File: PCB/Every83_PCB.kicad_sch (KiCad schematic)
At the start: 36 parts, among them IC2 GD25Q16, J1 781710004, J2 Conn_01x08_Pin, Q3 DMG2305, SW101 KMR2, SW102 KMR2, U2 AP2112(3.3V), U3 MCP73831T-2ACI/OT, X3 JSTPH, Y2 32.768

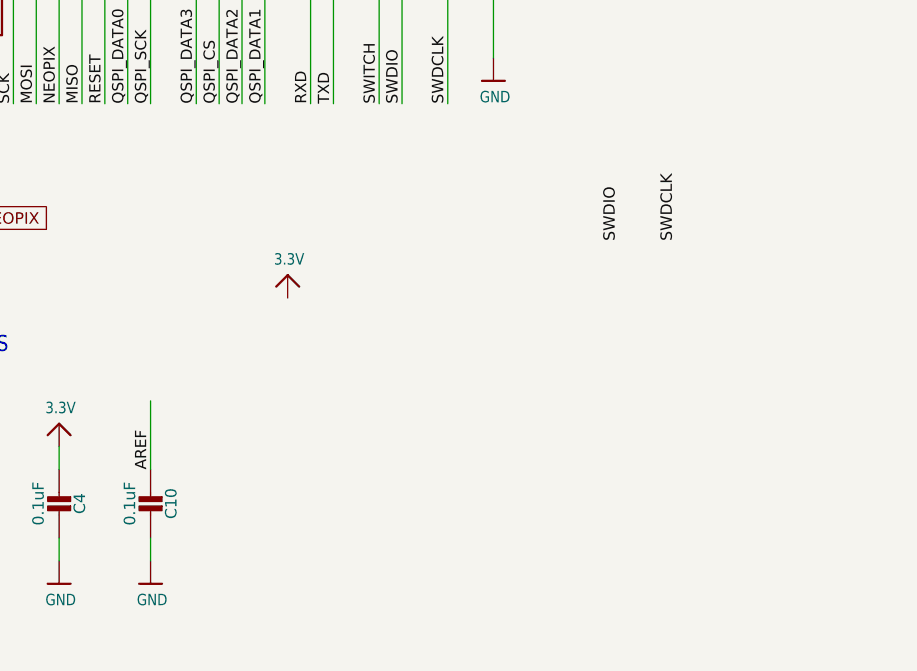
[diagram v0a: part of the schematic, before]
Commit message: update matrix nets and add swd footprint
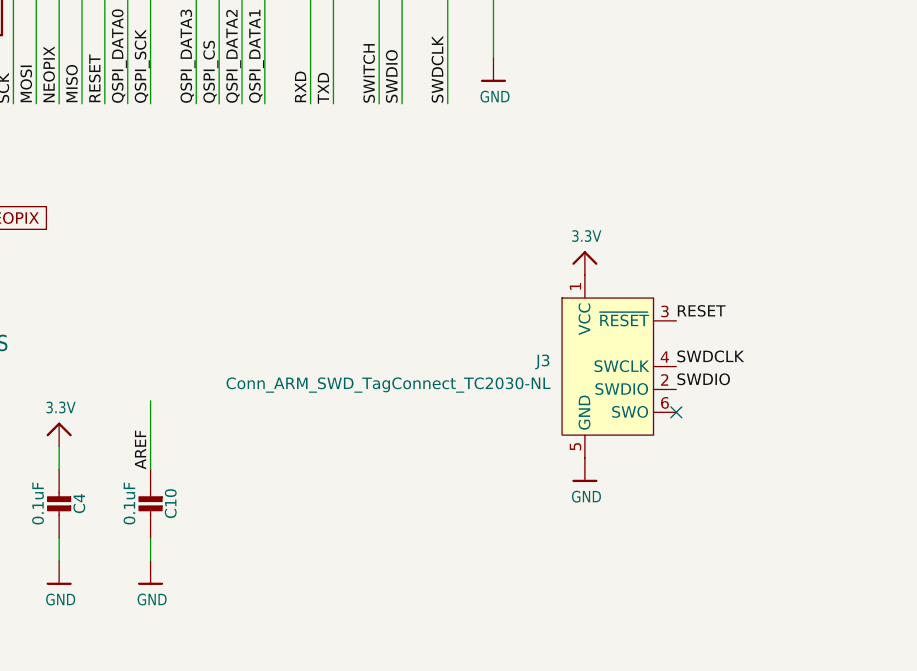
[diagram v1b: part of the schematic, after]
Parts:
- added J3: Conn_ARM_SWD_TagConnect_TC2030-NL, Connector:Tag-Connect_TC2030-IDC-NL_2x03_P1.27mm_Vertical, symbol Connector:Conn_ARM_SWD_TagConnect_TC2030-NL
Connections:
- net 3.3V: now also J3.1 (VCC)
- net GND: now also J3.5 (GND)
- net RESET: now also J3.3 (~{RESET})
- net SWDCLK: now also J3.4 (SWCLK)
- net SWDIO: now also J3.2 (SWDIO)
- no-connect marks 0 -> 1
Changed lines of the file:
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@@
   (junction (at 40.64 187.96) (diameter 0) (color 0 0 0 0)
   )
+  (no_connect (at 200.66 179.07))
   (wire (pts (xy 170.18 129.54) (xy 170.18 144.78))
     (stroke (width 0) (type default))
@@
     (effects (font (size 1.2446 1.2446)) (justify left bottom))
   )
+  (label "RESET" (at 200.66 168.91 0) (fields_autoplaced)
+    (effects (font (size 1.2446 1.2446)) (justify left bottom))
+  )
   (label "CS" (at 260.35 143.51 0) (fields_autoplaced)
     (effects (font (size 1.27 1.27)) (justify left bottom))
@@
     (effects (font (size 1.2446 1.2446)) (justify left bottom))
   )
-  (label "SWDIO" (at 194.31 160.02 90) (fields_autoplaced)
+  (label "SWDIO" (at 200.66 176.53 0) (fields_autoplaced)
     (effects (font (size 1.27 1.27)) (justify left bottom))
   )
@@
     (effects (font (size 1.27 1.27)) (justify left bottom))
   )
-  (label "SWDCLK" (at 200.66 160.02 90) (fields_autoplaced)
+  (label "SWDCLK" (at 200.66 173.99 0) (fields_autoplaced)
     (effects (font (size 1.27 1.27)) (justify left bottom))
   )
@@
         (path "/ea2432c4-eb7a-431a-b465-8c00cfcb4450"
           (reference "#U$018") (unit 1)
+        )
+      )
+    )
+  )
+  (symbol (lib_id "Adafruit nRF52840 Bluefruit Feather Express Rev D-eagle-import:GND") (at 190.5 186.69 0) (unit 1)
+    (in_bom yes) (on_board yes) (dnp no)
+    (property "Reference" "#U$024" (at 190.5 186.69 0)
+      (effects (font (size 1.27 1.27)) hide)
+    )
+    (property "Value" "GND" (at 188.976 189.23 0)
+      (effects (font (size 1.27 1.0795)) (justify left bottom))
+    )
+    (property "Footprint" "" (at 190.5 186.69 0)
+      (effects (font (size 1.27 1.27)) hide)
+    )
+    (property "Datasheet" "" (at 190.5 186.69 0)
+      (effects (font (size 1.27 1.27)) hide)
+    )
+    (pin "1")
+    (instances
+      (project "Every83_PCB"
+        (path "/ea2432c4-eb7a-431a-b465-8c00cfcb4450"
+          (reference "#U$024") (unit 1)
         )
       )
@@
     )
   )
-  (symbol (lib_id "Adafruit nRF52840 Bluefruit Feather Express Rev D-eagle-import:3.3V") (at 157.48 163.83 0) (unit 1)
-    (in_bom yes) (on_board yes) (dnp no)
-    (property "Reference" "#U$020" (at 157.48 163.83 0)
-      (effects (font (size 1.27 1.27)) hide)
-    )
-    (property "Value" "3.3V" (at 155.956 162.814 0)
-      (effects (font (size 1.27 1.0795)) (justify left bottom))
-    )
-    (property "Footprint" "" (at 157.48 163.83 0)
-      (effects (font (size 1.27 1.27)) hide)
-    )
-    (property "Datasheet" "" (at 157.48 163.83 0)
+  (symbol (lib_id "Adafruit nRF52840 Bluefruit Feather Express Rev D-eagle-import:3.3V") (at 190.5 161.29 0) (unit 1)
+    (in_bom yes) (on_board yes) (dnp no)
+    (property "Reference" "#U$020" (at 190.5 161.29 0)
+      (effects (font (size 1.27 1.27)) hide)
+    )
+    (property "Value" "3.3V" (at 188.976 160.274 0)
+      (effects (font (size 1.27 1.0795)) (justify left bottom))
+    )
+    (property "Footprint" "" (at 190.5 161.29 0)
+      (effects (font (size 1.27 1.27)) hide)
+    )
+    (property "Datasheet" "" (at 190.5 161.29 0)
       (effects (font (size 1.27 1.27)) hide)
     )
@@
         )
       )
+    )
+  )
+  (symbol (lib_id "Connector:Conn_ARM_SWD_TagConnect_TC2030-NL") (at 193.04 173.99 0) (unit 1)
+    (in_bom yes) (on_board yes) (dnp no) (fields_autoplaced)
+    (property "Reference" "J3" (at 186.69 173.355 0)
+      (effects (font (size 1.27 1.27)) (justify right))
+    )
+    (property "Value" "Conn_ARM_SWD_TagConnect_TC2030-NL" (at 186.69 175.895 0)
+      (effects (font (size 1.27 1.27)) (justify right))
+    )
+    (property "Footprint" "Connector:Tag-Connect_TC2030-IDC-NL_2x03_P1.27mm_Vertical" (at 193.04 191.77 0)
+      (effects (font (size 1.27 1.27)) hide)
+    )
+    (property "Datasheet" "https://www.tag-connect.com/wp-content/uploads/bsk-pdf-manager/TC2030-CTX_1.pdf" (at 193.04 189.23 0)
+      (effects (font (size 1.27 1.27)) hide)
+    )
+    (pin "1")
+    (pin "2")
+    (pin "3")
+    (pin "4")
+    (pin "5")
+    (pin "6")
+    (instances
+      (project "Every83_PCB"
+        (path "/ea2432c4-eb7a-431a-b465-8c00cfcb4450"
+          (reference "J3") (unit 1)
+        )
+      )

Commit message: Matrix work
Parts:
- removed C10: 0.1uF, Adafruit nRF52840 Bluefruit Feather Express Rev D:0603-NO, symbol Adafruit nRF52840 Bluefruit Feather Express Rev D-eagle-import:CAP_CERAMIC0603_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
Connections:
- net LED1: no longer MDBT1.8 (P1.15)
- net LED2: no longer MDBT1.3 (P1.10)
- net Col12: now reaches MDBT1.11 (P0.02/AIN0)
- net Col10: now reaches MDBT1.13 (P0.28/AIN4)
- net Col9: now reaches MDBT1.14 (P0.30/AIN6)
- net Col8: now reaches MDBT1.16 (P0.27)
- net Col7: now reaches MDBT1.19 (P0.26)
- net Col6: now reaches MDBT1.20 (P0.04/AIN2)
- net Col5: now reaches MDBT1.21 (P0.05/AIN3)
- net Col4: now reaches MDBT1.22 (P0.06)
- net Col3: now reaches MDBT1.23 (P0.07)
- net Col2: now reaches MDBT1.24 (P0.08)
- net Col1: now reaches MDBT1.25 (P1.08)
- net Col0: now reaches MDBT1.26 (P1.09)
- net Row3: now reaches MDBT1.4 (P1.11)
- net Row4: now reaches MDBT1.5 (P1.12)
- net Row5: now reaches MDBT1.6 (P1.13)
- net Row0: now reaches MDBT1.60 (P1.03)
- net Row1: now reaches MDBT1.61 (P1.01)
- net Col15: now reaches MDBT1.7 (P1.14)
- net Col13: now reaches MDBT1.9 (P0.03/AIN1)
- net AREF renamed Col11
- net SCL: no longer names the net of MDBT1.27 (P0.11)
- net SDA: no longer names the net of MDBT1.29 (P0.12)
- new net Col14: MDBT1.8 (P1.15)
- new net Row2: MDBT1.3 (P1.10)

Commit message: WIP
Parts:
- removed D103: ORANGE, Adafruit nRF52840 Bluefruit Feather Express Rev D:CHIPLED_0805_NOOUTLINE, symbol Adafruit nRF52840 Bluefruit Feather Express Rev D-eagle-import:LED0805_NOOUTLINE
- added D103: LED, Diode_SMD:D_0805_2012Metric_Pad1.15x1.40mm_HandSolder, symbol Device:LED
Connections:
- net VBUS: now also D103.2 (A)
- net at R3.1: now also D103.1 (K)
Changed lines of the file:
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@@
-    )
-  )
-  (symbol (lib_id "Adafruit nRF52840 Bluefruit Feather Express Rev D-eagle-import:LED0805_NOOUTLINE") (at 228.6 246.38 0) (unit 1)
-    (in_bom yes) (on_board yes) (dnp no)
-    (property "Reference" "D103" (at 227.33 241.935 0)
-      (effects (font (size 1.27 1.0795)))
-    )
-    (property "Value" "ORANGE" (at 227.33 249.174 0)
-      (effects (font (size 1.27 1.0795)))
-    )
-    (property "Footprint" "Adafruit nRF52840 Bluefruit Feather Express Rev D:CHIPLED_0805_NOOUTLINE" (at 228.6 246.38 0)
-      (effects (font (size 1.27 1.27)) hide)
-    )
-    (property "Datasheet" "" (at 228.6 246.38 0)
-      (effects (font (size 1.27 1.27)) hide)
-    )
-    (pin "A")
-    (pin "C")
-    (instances
-      (project "Every83_PCB"
-        (path "/ea2432c4-eb7a-431a-b465-8c00cfcb4450"
-          (reference "D103") (unit 1)
-        )
-      )
     )
   )
@@
         )
       )
+    )
+  )
+  (symbol (lib_id "Device:LED") (at 227.33 246.38 180) (unit 1)
+    (in_bom yes) (on_board yes) (dnp no) (fields_autoplaced)
+    (property "Reference" "D103" (at 228.9175 240.03 0)
+      (effects (font (size 1.27 1.27)))
+    )
+    (property "Value" "LED" (at 228.9175 242.57 0)
+      (effects (font (size 1.27 1.27)))
+    )
+    (property "Footprint" "Diode_SMD:D_0805_2012Metric_Pad1.15x1.40mm_HandSolder" (at 227.33 246.38 0)
+      (effects (font (size 1.27 1.27)) hide)
+    )
+    (property "Datasheet" "~" (at 227.33 246.38 0)
+      (effects (font (size 1.27 1.27)) hide)
+    )
+    (pin "1")
+    (pin "2")
+    (instances
+      (project "Every83_PCB"
+        (path "/ea2432c4-eb7a-431a-b465-8c00cfcb4450"
+          (reference "D103") (unit 1)
+        )
+      )

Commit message: Small work, moved the micro controller
Need to update the programming pins and add UART
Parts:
- removed J3: Conn_ARM_SWD_TagConnect_TC2030-NL, Connector:Tag-Connect_TC2030-IDC-NL_2x03_P1.27mm_Vertical, symbol Connector:Conn_ARM_SWD_TagConnect_TC2030-NL
- R4: value 4.7K -> 1.4k

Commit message: Some more matrix work
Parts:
- added J3, J4: SM03B-SRSS-TB, footprints:CONN_SM03B-SRSS-TB_JST, symbol 2024-03-25_01-24-54:SM03B-SRSS-TB
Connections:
- net Col0: now also MDBT1.16 (P0.27); no longer MDBT1.26 (P1.09)
- net Col1: now also MDBT1.20 (P0.04/AIN2); no longer MDBT1.25 (P1.08)
- net Col2: now also MDBT1.22 (P0.06); no longer MDBT1.24 (P0.08)
- net Col3: now also MDBT1.24 (P0.08); no longer MDBT1.23 (P0.07)
- net Col4: now also MDBT1.26 (P1.09); no longer MDBT1.22 (P0.06)
- net Col5: now also MDBT1.19 (P0.26); no longer MDBT1.21 (P0.05/AIN3)
- net Col6: now also MDBT1.21 (P0.05/AIN3); no longer MDBT1.20 (P0.04/AIN2)
- net Col7: now also MDBT1.23 (P0.07); no longer MDBT1.19 (P0.26)
- net Col8: now also MDBT1.25 (P1.08); no longer MDBT1.16 (P0.27)
- net GND: now also J3.2, J4.2
- net RXD: now also J4.1
- net SWDCLK: now also J3.1
- net SWDIO: now also J3.3
- net TXD: now also J4.3
- no-connect marks 1 -> 0

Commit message: Matrix should be done now
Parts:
- removed J2: Conn_01x08_Pin, Connector_PinHeader_1.00mm:PinHeader_1x08_P1.00mm_Vertical, symbol Connector:Conn_01x08_Pin
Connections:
- net BLK is gone; now on net Col0: MDBT1.56 (P1.04)
- net CS is gone; now on net Col3: MDBT1.59 (P1.05)
- net DC is gone; now on net Col1: MDBT1.57 (P1.06)
- net MISO is gone; now on net VDIV: MDBT1.39 (P0.15)
- net RES is gone; now on net Col2: MDBT1.58 (P1.07)
- net Col0: no longer MDBT1.16 (P0.27)
- net Col1: no longer MDBT1.20 (P0.04/AIN2)
- net Col10: now also MDBT1.9 (P0.03/AIN1); no longer MDBT1.13 (P0.28/AIN4)
- net Col11: now also MDBT1.10 (P0.29/AIN5); no longer MDBT1.12 (P0.31/AIN7)
- net Col13: now also MDBT1.12 (P0.31/AIN7); no longer MDBT1.9 (P0.03/AIN1)
- net Col14: now also MDBT1.14 (P0.30/AIN6); no longer MDBT1.8 (P1.15)
- net Col15: now also MDBT1.13 (P0.28/AIN4); no longer MDBT1.7 (P1.14)
- net Col2: no longer MDBT1.22 (P0.06)
- net Col3: no longer MDBT1.24 (P0.08)
- net Col4: now also MDBT1.3 (P1.10); no longer MDBT1.26 (P1.09)
- net Col5: now also MDBT1.4 (P1.11); no longer MDBT1.19 (P0.26)
- net Col6: now also MDBT1.5 (P1.12); no longer MDBT1.21 (P0.05/AIN3)
- net Col7: now also MDBT1.6 (P1.13); no longer MDBT1.23 (P0.07)
- net Col8: now also MDBT1.7 (P1.14); no longer MDBT1.25 (P1.08)
- net Col9: now also MDBT1.8 (P1.15); no longer MDBT1.14 (P0.30/AIN6)
- net Row0: now also MDBT1.22 (P0.06); no longer MDBT1.60 (P1.03)
- net Row1: now also MDBT1.23 (P0.07); no longer MDBT1.61 (P1.01)
- net Row2: now also MDBT1.24 (P0.08); no longer MDBT1.3 (P1.10)
- net Row3: now also MDBT1.25 (P1.08); no longer MDBT1.4 (P1.11)
- net Row4: now also MDBT1.26 (P1.09); no longer MDBT1.5 (P1.12)
- net Row5: now also MDBT1.27 (P0.11); no longer MDBT1.6 (P1.13)
- net VDIV: no longer MDBT1.10 (P0.29/AIN5)
- net MOSI: no longer names the net of MDBT1.37 (P0.13)
- net SCK: no longer names the net of MDBT1.36 (P0.14)

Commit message: missed something
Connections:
- net Row0: now also MDBT1.16 (P0.27); no longer MDBT1.22 (P0.06)
- net Row1: now also MDBT1.20 (P0.04/AIN2); no longer MDBT1.23 (P0.07)
- net Row2: now also MDBT1.22 (P0.06); no longer MDBT1.24 (P0.08)
- net Row3: now also MDBT1.24 (P0.08); no longer MDBT1.25 (P1.08)
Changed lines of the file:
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@@
 	(global_label "Row3"
 		(shape input)
-		(at 101.6 101.6 180)
-		(fields_autoplaced yes)
-		(effects
-			(font
-				(size 1.27 1.27)
-			)
-			(justify right)
-		)
-		(property "Intersheetrefs" "${INTERSHEET_REFS}"
-			(at 93.6558 101.6 0)
+		(at 101.6 99.06 180)
+		(fields_autoplaced yes)
+		(effects
+			(font
+				(size 1.27 1.27)
+			)
+			(justify right)
+		)
+		(property "Intersheetrefs" "${INTERSHEET_REFS}"
+			(at 93.6558 99.06 0)
 			(effects
 				(font
@@
 	(global_label "Row0"
 		(shape input)
+		(at 101.6 78.74 180)
+		(fields_autoplaced yes)
+		(effects
+			(font
+				(size 1.27 1.27)
+			)
+			(justify right)
+		)
+		(property "Intersheetrefs" "${INTERSHEET_REFS}"
+			(at 93.6558 78.74 0)
+			(effects
+				(font
+					(size 1.27 1.27)
+				)
+				(justify right)
+				(hide yes)
+			)
+		)
+	)
+	(global_label "Col9"
+		(shape input)
+		(at 149.86 68.58 90)
+		(fields_autoplaced yes)
+		(effects
+			(font
+				(size 1.27 1.27)
+			)
+			(justify left)
+		)
+		(property "Intersheetrefs" "${INTERSHEET_REFS}"
+			(at 149.86 61.3805 90)
+			(effects
+				(font
+					(size 1.27 1.27)
+				)
+				(justify left)
+				(hide yes)
+			)
+		)
+	)
+	(global_label "Row2"
+		(shape input)
 		(at 101.6 93.98 180)
 		(fields_autoplaced yes)
@@
 		)
 	)
-	(global_label "Col9"
-		(shape input)
-		(at 149.86 68.58 90)
-		(fields_autoplaced yes)
-		(effects
-			(font
-				(size 1.27 1.27)
-			)
-			(justify left)
-		)
-		(property "Intersheetrefs" "${INTERSHEET_REFS}"
-			(at 149.86 61.3805 90)
-			(effects
-				(font
-					(size 1.27 1.27)
-				)
-				(justify left)
-				(hide yes)
-			)
-		)
-	)
-	(global_label "Row2"
-		(shape input)
-		(at 101.6 99.06 180)
-		(fields_autoplaced yes)
-		(effects
-			(font
-				(size 1.27 1.27)
-			)
-			(justify right)
-		)
-		(property "Intersheetrefs" "${INTERSHEET_REFS}"
-			(at 93.6558 99.06 0)
-			(effects
-				(font
-					(size 1.27 1.27)
-				)
-				(justify right)
-				(hide yes)
-			)
-		)
-	)
 	(global_label "Col13"
 		(shape input)
@@
 	(global_label "Row1"
 		(shape input)
-		(at 101.6 96.52 180)
-		(fields_autoplaced yes)
-		(effects
-			(font
-				(size 1.27 1.27)
-			)
-			(justify right)
-		)
-		(property "Intersheetrefs" "${INTERSHEET_REFS}"
-			(at 93.6558 96.52 0)
-			(effects
-				(font
+		(at 101.6 88.9 180)
+		(fields_autoplaced yes)
+		(effects
+			(font
+				(size 1.27 1.27)
+			)
+			(justify right)
+		)
+		(property "Intersheetrefs" "${INTERSHEET_REFS}"
+			(at 93.6558 88.9 0)
+			(effects
+				(font

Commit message: swap micro
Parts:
- removed C1, C2: 22pF, Adafruit nRF52840 Bluefruit Feather Express Rev D:0603-NO, symbol Adafruit nRF52840 Bluefruit Feather Express Rev D-eagle-import:CAP_CERAMIC0603_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
- removed IC2: GD25Q16, Adafruit nRF52840 Bluefruit Feather Express Rev D:USON8, symbol Adafruit nRF52840 Bluefruit Feather Express Rev D-eagle-import:SPIFLASH_8PINUX
- removed L1: DNP, Adafruit nRF52840 Bluefruit Feather Express Rev D:_0805MP, symbol Adafruit nRF52840 Bluefruit Feather Express Rev D-eagle-import:INDUCTOR_0805MP
- removed MDBT1: MDBT50, Adafruit nRF52840 Bluefruit Feather Express Rev D:MDBT50, symbol Adafruit nRF52840 Bluefruit Feather Express Rev D-eagle-import:MDBT50
- removed Y2: 32.768, Adafruit nRF52840 Bluefruit Feather Express Rev D:XTAL3215, symbol Adafruit nRF52840 Bluefruit Feather Express Rev D-eagle-import:XTAL-3.2X1.5
- added U1: ~, symbol JohnDeere:Core52480
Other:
- note removed: "16MBIT QSPI FLASH"
- note removed: "Place 10uH for DC/DC"
